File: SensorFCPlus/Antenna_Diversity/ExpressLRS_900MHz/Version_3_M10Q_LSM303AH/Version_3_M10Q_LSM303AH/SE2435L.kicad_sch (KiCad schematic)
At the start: 23 parts, among them U6 SE2435L

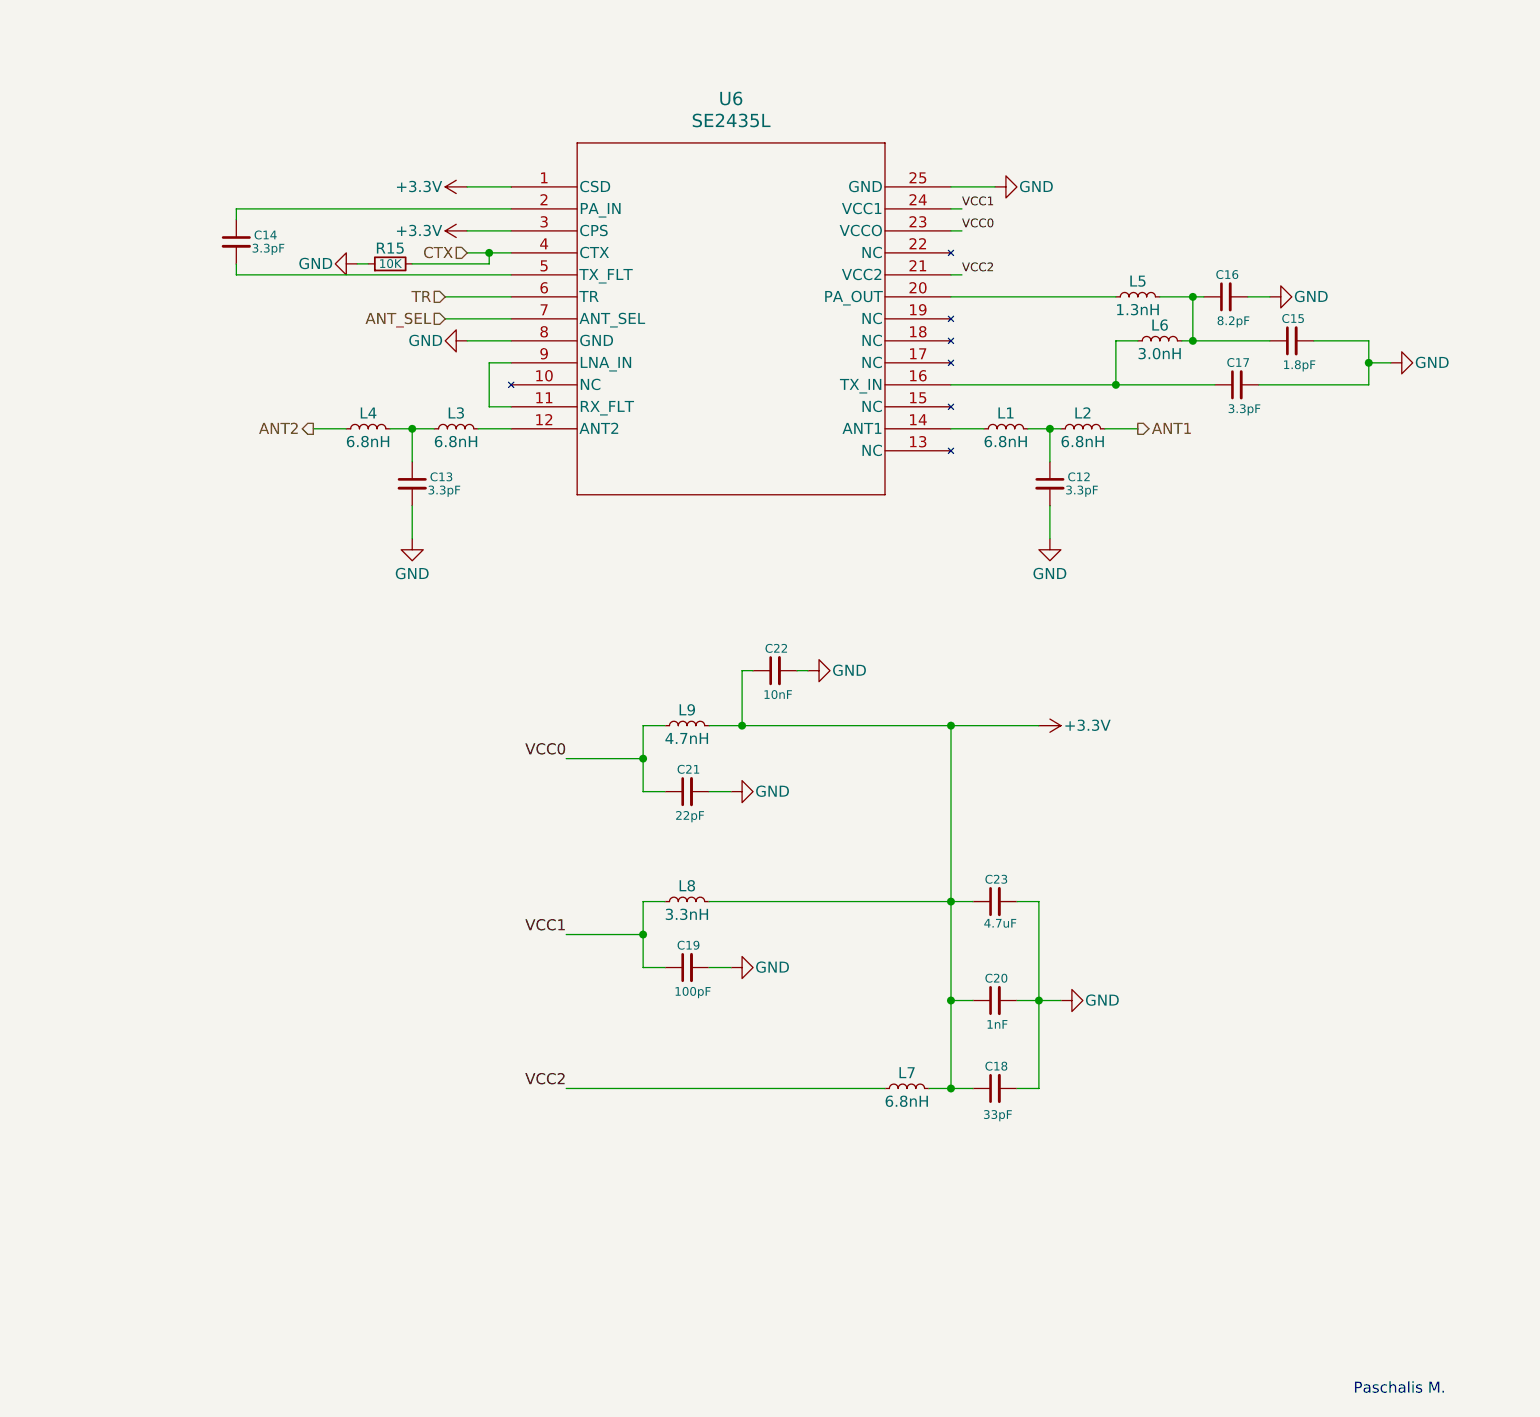
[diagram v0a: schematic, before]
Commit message: Update KiCad files for ExpressLRS modules
- Modified:
  - 2.4GHz Version 3 (M10Q LSM303AH) project and schematic files
  - 900MHz Version 3 (M10Q LSM303AH) schematic files for ESP8285 and SE2435L

- Added:
  - 2.4GHz Version 3 schematics: ESP8285, SE2431, SE2431L, SX1280
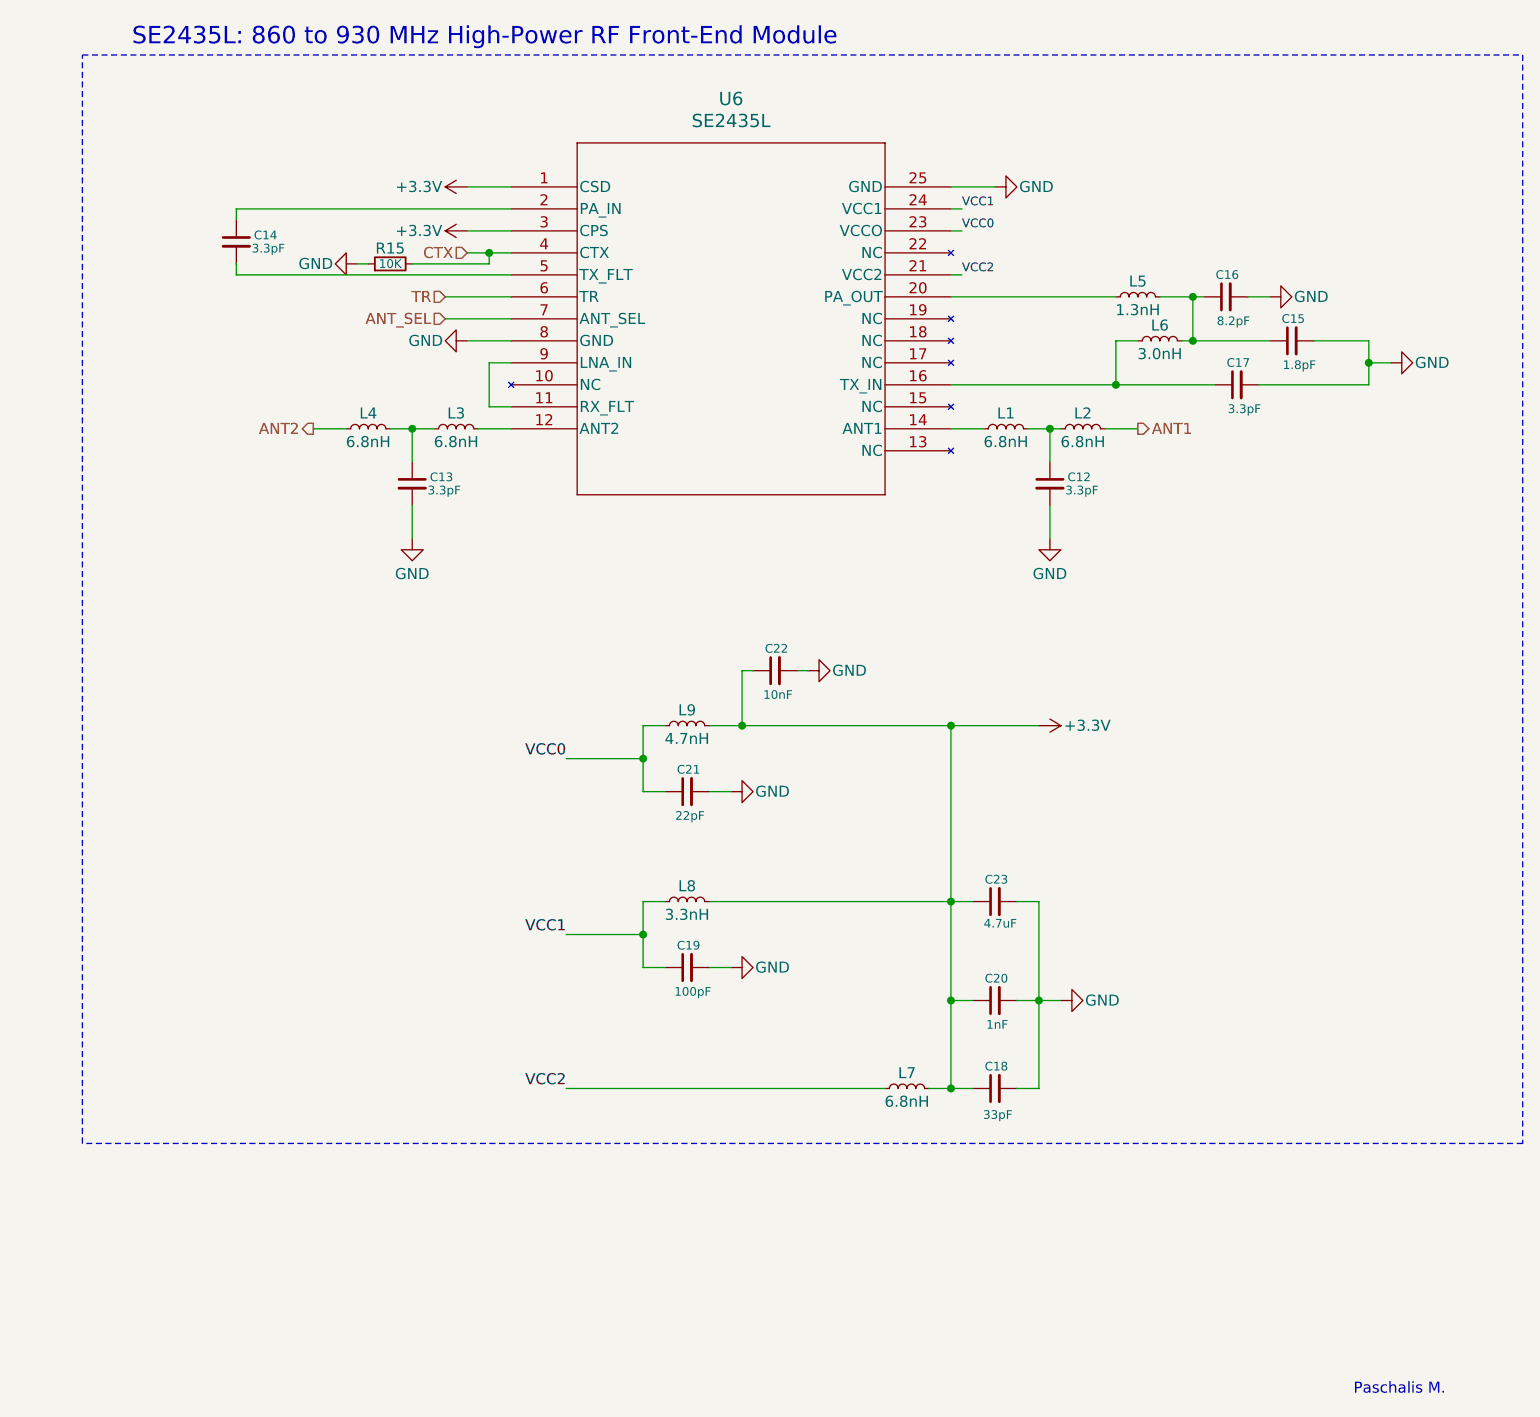
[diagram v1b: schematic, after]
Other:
- note added: "SE2435L: 860 to 930 MHz High-Power RF Front-End Module"
- title: SE435L (860 to 930 MHz High-Power RF Front-End Module) -> SE2435L (860 to 930 MHz High-Power RF Front-End Module)
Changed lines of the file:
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@@
 	(paper "A4")
 	(title_block
-		(title "SE435L (860 to 930 MHz High-Power RF Front-End Module)")
+		(title "SE2435L (860 to 930 MHz High-Power RF Front-End Module)")
 		(date "06-01-2025")
 		(rev "1.0")
@@
 			(width 0)
 			(type default)
+		)
+	)
+	(rectangle
+		(start 62.23 29.21)
+		(end 228.6 154.94)
+		(stroke
+			(width 0)
+			(type dash)
+		)
+		(fill
+			(type none)
 		)
 	)
@@
 			)
 		)
+	)
+	(text "SE2435L: 860 to 930 MHz High-Power RF Front-End Module"
+		(exclude_from_sim no)
+		(at 108.712 27.178 0)
+		(effects
+			(font
+				(size 2 2)
+			)
+		)
